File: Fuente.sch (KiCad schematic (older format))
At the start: 9 parts, among them U1 XL4005E1

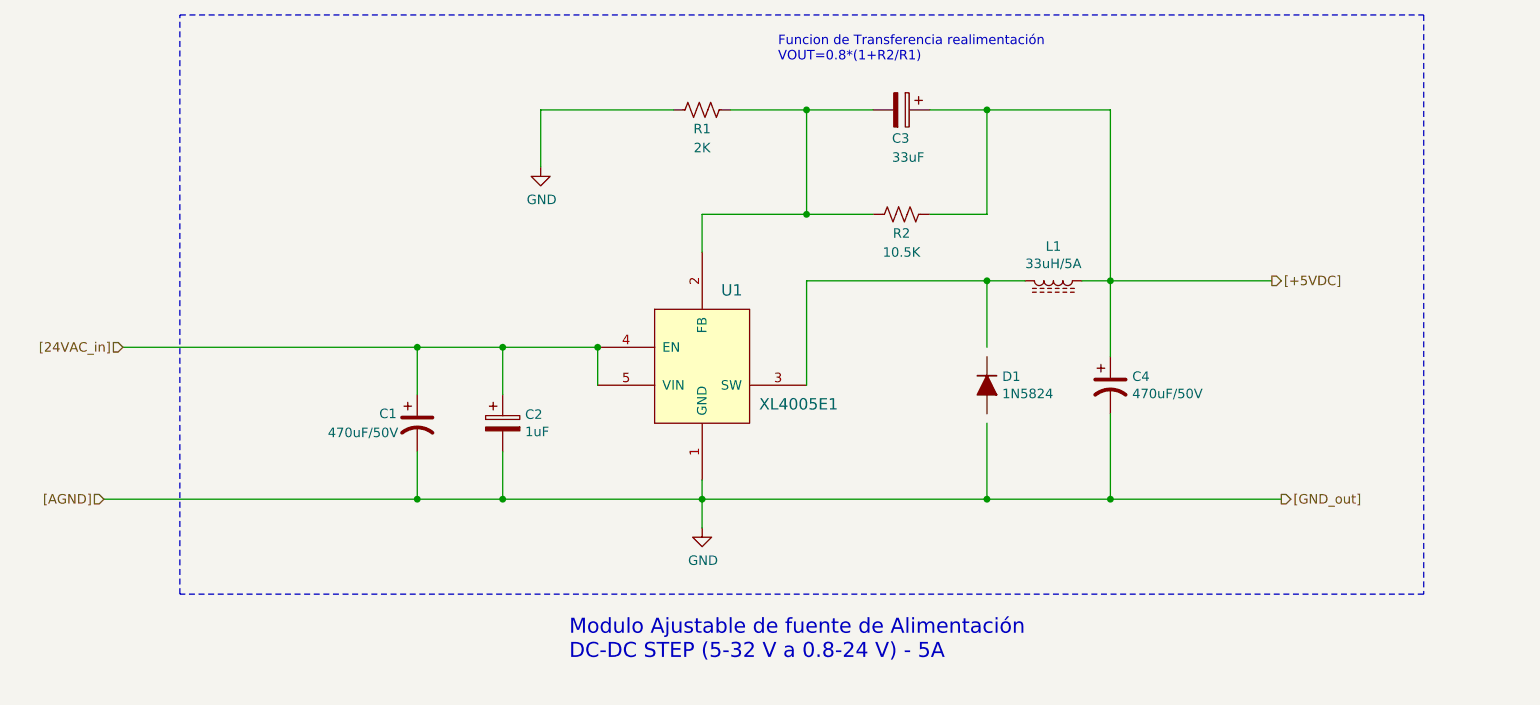
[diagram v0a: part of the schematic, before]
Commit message: Agregado puente diodo
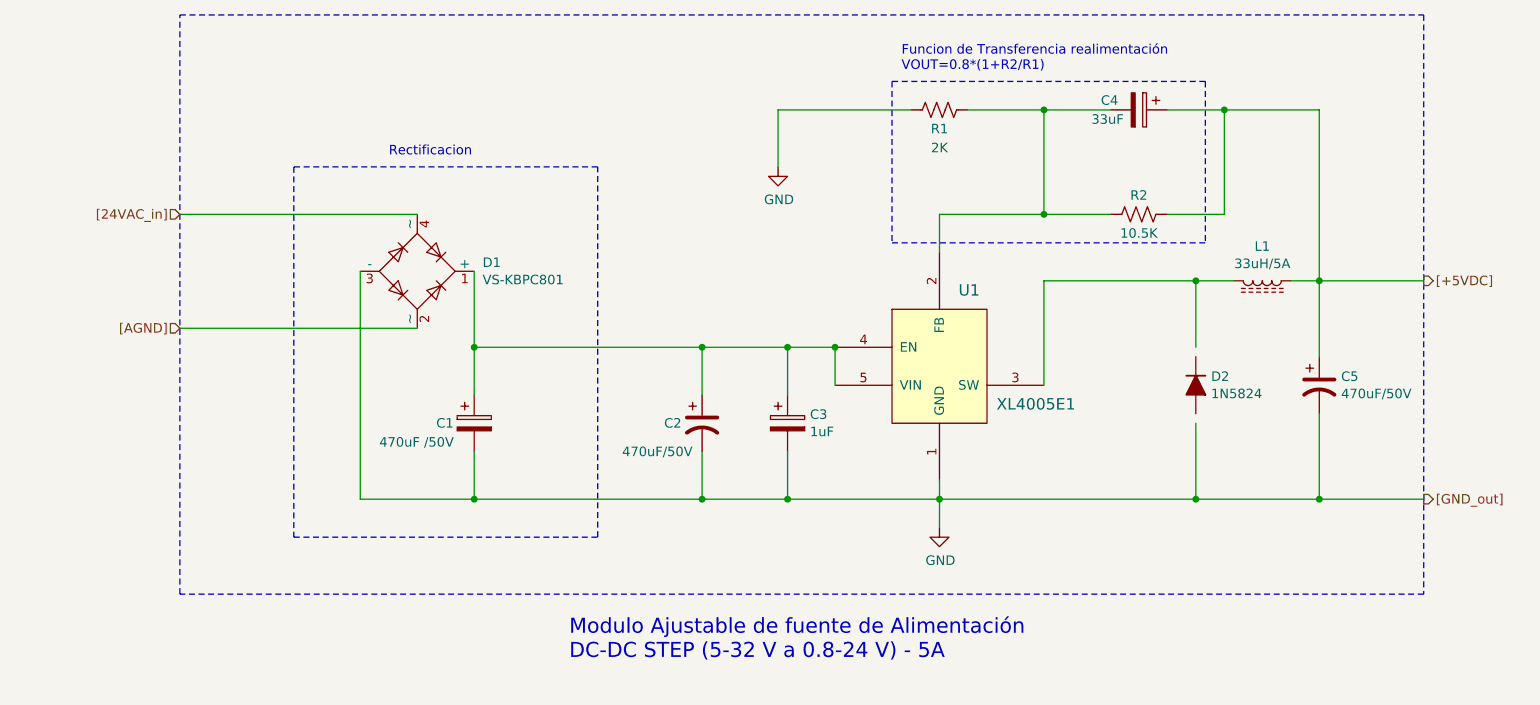
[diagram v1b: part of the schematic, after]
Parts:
- added C1: 470uF /50V, symbol Device:CP
- added D1: VS-KBPC801, Diode_THT:Diode_Bridge_Vishay_KBPC6, symbol Diode_Bridge:VS-KBPC801
- renumbered C1 to C2, C2 to C3, C3 to C4, C4 to C5, D1 to D2
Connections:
- wire segments 38 -> 45
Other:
- note added: "Rectificacion"
- moved on the sheet: C2, C3, C4, C5, D2, L1, R1, R2, U1

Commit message: Agregado fuente 3.3V
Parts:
- added C? (x5): 470uF /50V, symbol Device:CP
- added D?: D, symbol Device:D
- added IC?: MP1584EN-LF, SOIC127P600X170-9N, symbol 00_lib_sch:MP1584EN-LF
- added L?: L, symbol Device:L
- added R? (x6): 10.5K, symbol Device:R_US
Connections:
- wire segments 45 -> 84
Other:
- note added: "Curva de eficiencia"
- moved on the sheet: C1, C2, C3, C4, C5, D1, D2, L1, R1, R2, U1

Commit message: Arreglo raiz de proyecto
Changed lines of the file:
@@
 	9800 4900 11050 4900
 Wire Notes Line
-	11100 5600 11100 6450
-Wire Notes Line
-	11100 6450 9850 6450
+	11050 4900 11050 5750
+Wire Notes Line
+	11050 5750 9800 5750
 Wire Notes Line
 	9800 5750 9800 4900
-Text Notes 9950 6100 0    50   ~ 0
+Text Notes 9900 5400 0    50   ~ 0
 INVESTIGAR REGULADOR O \nFUENTE SWTH, 3,3V PARA\nSENSORES  y ESP32
 Wire Wire Line
@@
 Data
 89 50 4E 47 0D 0A 1A 0A 00 00 00 0D 49 48 44 52 00 00 02 3D 00 00 02 68 08 02 00 00 00 02 B0 C7
-12 00 00 00 03 73 42 49 54 08 08 08 DB E1 4F E0 00 00 00 09 70 48 59 73 00 00 0E C3 00 00 0E C3
-01 C7 6F A8 64 00 00 20 00 49 44 41 54 78 9C EC BD 77 B4 1C D7 75 E6 FB ED 7D 4E 55 75 F7 8D B8
+12 00 00 00 03 73 42 49 54 08 08 08 DB E1 4F E0 00 00 00 09 70 48 59 73 00 00 0E 74 00 00 0E 74
+01 6B 24 B3 D6 00 00 20 00 49 44 41 54 78 9C EC BD 77 B4 1C D7 75 E6 FB ED 7D 4E 55 75 F7 8D B8
 17 39 E7 9C 03 09 82 59 A4 48 81 22 29 91 94 A8 2C 79 AC 60 39 CD D3 58 F6 93 47 CF 1E 8D C6 CF
 F3 3C 63 8F ED 19 5B 96 25 4B 96 25 59 99 14 83 48 30 81 09 04 01 92 20 12 11 08 22 27 22 C7 9B

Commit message: Fuente 3v3 agregada
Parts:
- removed C? (x5): 470uF /50V, symbol Device:CP
- removed D?: D, symbol Device:D
- removed IC?: MP1584EN-LF, SOIC127P600X170-9N, symbol 00_lib_sch:MP1584EN-LF
- removed L?: L, symbol Device:L
- removed R? (x6): 10.5K, symbol Device:R_US
- added C202, C208: 470uF/50V, symbol Device:CP1
- added C204: 1uF, symbol Device:CP
- added C206: 33uF, symbol Device:CP
- added D202: 1N5824, DIOAD1898W129L762D1143, symbol 00_lib_sch:1N5824
- added L202: 33uH/5A, symbol Device:L_Core_Ferrite
- added R202: 4K7, symbol Device:R_US
- added R204: 15K, symbol Device:R_US
- added TP201, TP202: TestPoint_2Pole, symbol Connector:TestPoint_2Pole
- added U202: XL4005E1, symbol 00_lib_sch:XL4005E1
- C209: renamed from C1; value 470uF /50V -> 470uF/50V
- R201: renamed from R1; value 2K -> 1K5
- R203: renamed from R2; value 10.5K -> 8K2
- renumbered C2 to C201, C3 to C203, C4 to C205, C5 to C207, D2 to D201, D1 to D203, L1 to L201, U1 to U201
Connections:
- net labels added: 24V_CC, 24_CC
- wire segments 84 -> 85
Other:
- note removed: "Curva de eficiencia"
- note removed: "INVESTIGAR REGULADOR O \nFUENTE SWTH, 3,3V PARA\nSENSORES y ESP32"
- moved on the sheet: C201, C203, C205, C207, C209, D201, D203, L201, R201, R203, U201

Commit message: Agrego v1.0 de SmartSaffron
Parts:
- removed C203, C204: 1uF, symbol Device:CP
- removed C205, C206: 33uF, symbol Device:CP
- removed C209: 470uF/50V, symbol Device:CP
- removed D203: VS-KBPC801, Diode_THT:Diode_Bridge_Vishay_KBPC6, symbol Diode_Bridge:VS-KBPC801
- removed R201: 1K5, symbol Device:R_US
- removed R202: 4K7, symbol Device:R_US
- removed R203: 8K2, symbol Device:R_US
- removed R204: 15K, symbol Device:R_US
- removed TP201, TP202: TestPoint_2Pole, symbol Connector:TestPoint_2Pole
- added C101: 470uF/50V, 00_lib_fp:CP_Elec_10x10, symbol Device:CP1
- added C102, C106: 33u, 00_lib_fp:C_0805_2012Metric_Pad1.18x1.45mm_HandSolder, symbol 00_lib_sch:C
- added C105, C109: 1u, 00_lib_fp:C_0805_2012Metric_Pad1.18x1.45mm_HandSolder, symbol 00_lib_sch:C
- added D101: DF06S, 00_lib_fp:Diode_Bridge_Vishay_DFSFlat, symbol 00_lib_sch:DF06S
- added D103, D105: green, 00_lib_fp:LED_0805_2012Metric_Castellated, symbol 00_lib_sch:LED_ALT
- added JP101, JP102, JP103, JP104: jumper, 00_lib_fp:SolderJumper-2_P1.3mm_Open_RoundedPad1.0x1.5mm, symbol 00_lib_sch:jumper
- added R101: 1k5, 00_lib_fp:R_0805_2012Metric_Pad1.20x1.40mm_HandSolder, symbol 00_lib_sch:R
- added R102, R103, R107, R108: 0, 00_lib_fp:R_0805_2012Metric_Pad1.20x1.40mm_HandSolder, symbol 00_lib_sch:R
- added R104: 8k2, 00_lib_fp:R_0805_2012Metric_Pad1.20x1.40mm_HandSolder, symbol 00_lib_sch:R
- added R105, R110: 2k2, 00_lib_fp:R_0805_2012Metric_Pad1.20x1.40mm_HandSolder, symbol 00_lib_sch:R
- added R106: 4k7, 00_lib_fp:R_0805_2012Metric_Pad1.20x1.40mm_HandSolder, symbol 00_lib_sch:R
- added R109: 15k, 00_lib_fp:R_0805_2012Metric_Pad1.20x1.40mm_HandSolder, symbol 00_lib_sch:R
- C103: renamed from C207; footprint (none) -> 00_lib_fp:CP_Elec_8x10.5
- C104: renamed from C201; value 470uF/50V -> 470u/50V; footprint (none) -> 00_lib_fp:CP_Elec_8x10.5
- C107: renamed from C208; footprint (none) -> 00_lib_fp:CP_Elec_8x10.5
- C108: renamed from C202; footprint (none) -> 00_lib_fp:CP_Elec_8x10.5
- D102: renamed from D201; footprint DIOAD1898W129L762D1143 -> 00_lib_fp:D_SMB_Handsoldering
- D104: renamed from D202; footprint DIOAD1898W129L762D1143 -> 00_lib_fp:D_SMB_Handsoldering
- L101: renamed from L201; footprint (none) -> 00_lib_fp:Coil_ferrite
- L102: renamed from L202; footprint (none) -> 00_lib_fp:Coil_ferrite
- U101: renamed from U201; footprint (none) -> 00_lib_fp:TO-263-5_TabPin3
- U102: renamed from U202; footprint (none) -> 00_lib_fp:TO-263-5_TabPin3
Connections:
- net labels added: 24V_DC
- net labels removed: 24V_CC, 24_CC
- wire segments 85 -> 127
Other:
- note added: "DC-DC STEP-DOWN \n3V3-5A"
- note added: "DC-DC STEP-DOWN \n5V-5A"
- note added: "Funcion de Transferencia realimentacion\nVOUT=0.8*(1+R2/R1)"
- note added: "Funcion de transferencia realimentación\nVOUT=0.8*(1+R2/R1)"
- note added: "POWER"
- note added: "Pin Configuration"
- note removed: "Funcion de Transferencia realimentación\nVOUT=0.8*(1+R2/R1)"
- note removed: "Modulo Ajustable de fuente de Alimentación\nDC-DC STEP (5-32 V a 0.8-24 V) - 5A"
- moved on the sheet: C103, C104, C107, C108, D102, D104, L101, L102, U101, U102

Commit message: Revision
    * Acomodo los datos de F.Fab y B.Fab
    * Genero ibom
    * Exporto PDF e imagenes
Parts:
- C101, C108: value 470uF/50V -> 470u/50V
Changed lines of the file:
@@
 P 1700 6400
 F 0 "C108" H 1400 6450 50  0000 L CNN
-F 1 "470uF/50V" H 1600 6350 50  0000 R CNN
+F 1 "470u/50V" H 1600 6350 50  0000 R CNN
 F 2 "00_lib_fp:CP_Elec_8x10.5" H 1700 6400 50  0001 C CNN
 F 3 "~" H 1700 6400 50  0001 C CNN
@@
 U 1 1 61A488D3
 P 4300 1250
-F 0 "C101" H 4000 1300 50  0000 L CNN
-F 1 "470uF/50V" H 4200 1200 50  0000 R CNN
+F 0 "C101" H 3925 1250 50  0000 L CNN
+F 1 "470u/50V" H 4300 1125 50  0000 R CNN
 F 2 "00_lib_fp:CP_Elec_10x10" H 4300 1250 50  0001 C CNN
 F 3 "~" H 4300 1250 50  0001 C CNN

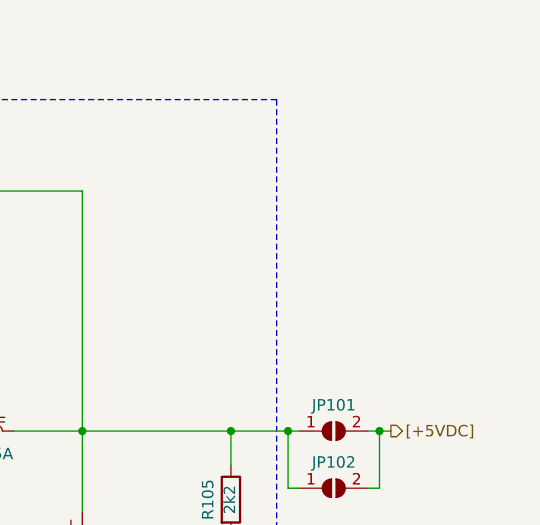
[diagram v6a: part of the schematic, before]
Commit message: Fix por revision grupal
    *Fix de memoria de i2c, mal sda y scl
    *Fix inpunts sda y scl
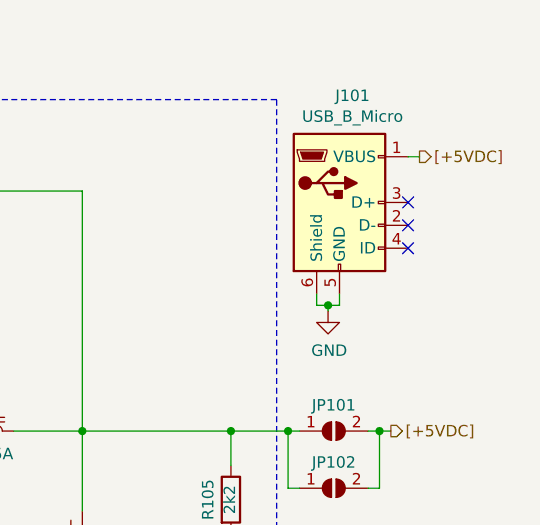
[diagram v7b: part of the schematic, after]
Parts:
- added J101: USB_B_Micro, 00_lib_fp:USB_Micro-B_Molex_47346-0001, symbol Connector:USB_B_Micro
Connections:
- net GND: now also J101.5 (GND), J101.6 (Shield)
- net [+5VDC]: now also J101.1 (VBUS)
- no-connect marks 0 -> 3
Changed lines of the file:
@@
 Connection ~ 10000 2500
 Wire Wire Line
-	10000 2500 10250 2500
-Wire Wire Line
 	10000 3350 10000 3500
 Connection ~ 10000 3500
@@
 Wire Notes Line
 	7000 2150 8750 2150
+$Comp
+L power:GND #PWR0249
+U 1 1 617207FB
+P 10425 1975
+F 0 "#PWR0249" H 10425 1725 50  0001 C CNN
+F 1 "GND" H 10430 1802 50  0000 C CNN
+F 2 "" H 10425 1975 50  0001 C CNN
+F 3 "" H 10425 1975 50  0001 C CNN
+	1    10425 1975
+	1    0    0    -1
+$EndComp
+Wire Wire Line
+	10425 1975 10425 1950
+Wire Wire Line
+	10425 1950 10375 1950
+Wire Wire Line
+	10375 1950 10375 1900
+Wire Wire Line
+	10425 1950 10475 1950
+Wire Wire Line
+	10475 1950 10475 1900
+Connection ~ 10425 1950
+NoConn ~ 10775 1500
+NoConn ~ 10775 1600
+Wire Wire Line
+	10000 2500 10250 2500
+Text HLabel 10825 1300 2    50   Output ~ 0
+[+5VDC]
+Wire Wire Line
+	10825 1300 10775 1300
+$Comp
+L Connector:USB_B_Micro J101
+U 1 1 61780319
+P 10475 1500
+F 0 "J101" H 10532 1967 50  0000 C CNN
+F 1 "USB_B_Micro" H 10532 1876 50  0000 C CNN
+F 2 "00_lib_fp:USB_Micro-B_Molex_47346-0001" H 10625 1450 50  0001 C CNN
+F 3 "~" H 10625 1450 50  0001 C CNN
+	1    10475 1500
+	1    0    0    -1
+$EndComp
+NoConn ~ 10775 1700
 $EndSCHEMATC
